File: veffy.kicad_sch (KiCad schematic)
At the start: 134 parts, among them CN1 XH-2AW_C2908611, J1 SWD, J2 Conn_Coaxial, J3 USB_C_Receptacle_USB2.0_14P, Q1 2N7002, Q2 BFR93A, Q3 2N7002, Q4 BFR93AE6327HTSA1, SW1 SW_Push, SW2 SW_Push, U1 ATSAMD21G18A-A, U10 MC34063AD, U11 AP2112K-3.3, U2 ADF4112BCPZ, U3 SA612AN/01_112, U4 MC3361, U5 LM386, U6 LM358_DFN, U7 AD9834, U8 QPA9510, U9 MCP73831-2-OT, Y2 C7527392

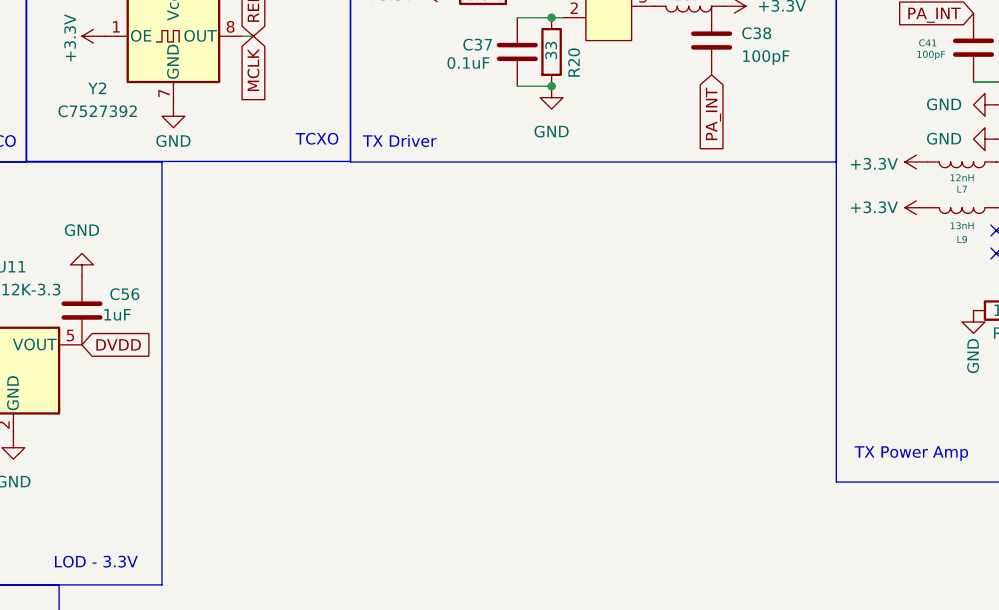
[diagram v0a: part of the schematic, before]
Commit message: TX Bandpass filter done
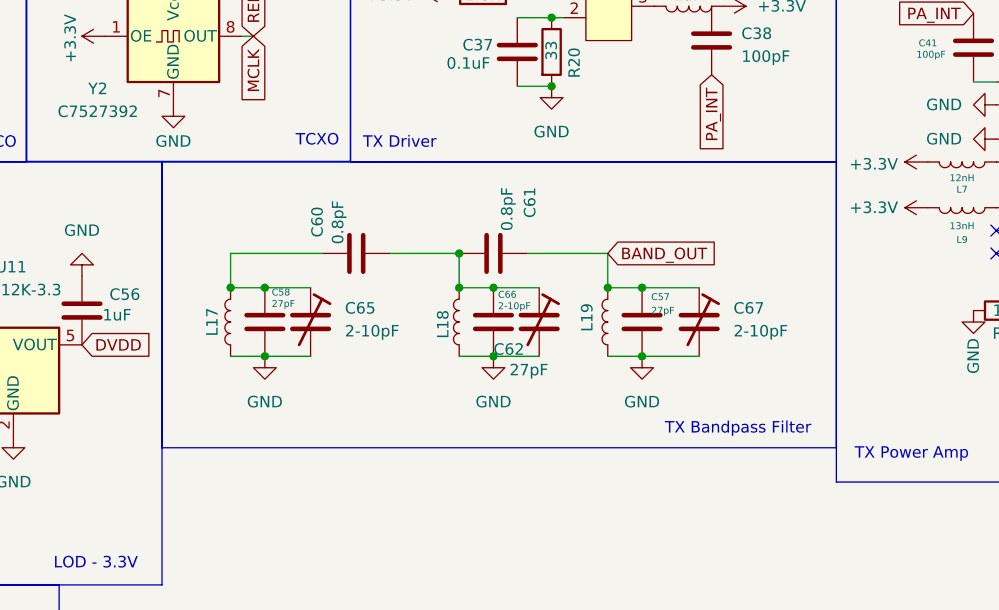
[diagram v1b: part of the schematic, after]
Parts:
- added C57, C58, C62: 27pF, symbol Device:C
- added C60, C61: 0.8pF, symbol Device:C
- added C65, C66, C67: 2-10pF, symbol Device:C_Trim
- added L17, L18, L19: 0603CS-33NXJLW, symbol Device:L
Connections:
- net BAND_OUT: now also C57.1, C61.1, C67.1, L19.2
- net GND: now also C57.2, C58.2, C62.2, C65.2, C66.2, C67.2, L17.1, L18.1, L19.1
- new net: C60.1, C61.2, C62.1, C66.1, L18.2
- new net: C58.1, C60.2, C65.1, L17.2
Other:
- note added: "TX Bandpass Filter"

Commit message: schematic fixes
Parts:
- added unit 1 of U6
- added unit 3 of U6
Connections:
- net +3.3V: now also C38.1, U6.8 (V+)
- net GND: now also C42.2, U6.3 (+), U6.4 (V-)
- net PRE_AMP: now also U6.7; no longer U6.1
- net RX_MIX_INT: now also U3.1 (INPUTA)
- net SPEAKER: now also R4.1
- net at R6.1, R7.1: now also U6.6 (-); no longer U6.2 (-)
- net at C19.1, L2.2: now also C42.1
- net at C25.2: now also U6.5 (+); no longer U6.3 (+)
- net at C22.1: now also U5.5
- new net: U6.1, U6.2 (-)
- no-connect marks 16 -> 17
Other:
- moved on the sheet: C16, C17, C18, C19, C23, C24, C38, C50, L16, L2, R4, U4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

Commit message: fixes
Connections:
- net +3.3V: no longer C38.1
- net IF_455K: now also C58.1, C60.2, C65.1, L17.2
- net at LRFC2.2, Q4.3: now also C38.1
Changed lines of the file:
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@@
 	)
 	(junction
+		(at 205.74 161.29)
+		(diameter 0)
+		(color 0 0 0 0)
+	)
+	(junction
 		(at 232.41 97.79)
 		(diameter 0)
@@
 	)
 	(junction
-		(at 213.36 161.29)
-		(diameter 0)
-		(color 0 0 0 0)
-	)
-	(junction
 		(at 50.8 125.73)
 		(diameter 0)
@@
 		)
 	)
+	(global_label "DVDD"
+		(shape input)
+		(at 213.36 161.29 0)
+		(fields_autoplaced yes)
+		(effects
+			(font
+				(size 1.27 1.27)
+			)
+			(justify left)
+		)
+		(property "Intersheetrefs" "${INTERSHEET_REFS}"
+			(at 221.2438 161.29 0)
+			(hide yes)
+			(show_name no)
+			(do_not_autoplace no)
+			(effects
+				(font
+					(size 1.27 1.27)
+				)
+				(justify left)
+			)
+		)
+	)
 	(global_label "VCO_OUT"
 		(shape input)
@@
 		)
 	)
+	(global_label "PA_INT"
+		(shape input)
+		(at 205.74 168.91 270)
+		(fields_autoplaced yes)
+		(effects
+			(font
+				(size 1.27 1.27)
+			)
+			(justify right)
+		)
+		(property "Intersheetrefs" "${INTERSHEET_REFS}"
+			(at 205.74 178.1243 90)
+			(hide yes)
+			(show_name no)
+			(do_not_autoplace no)
+			(effects
+				(font
+					(size 1.27 1.27)
+				)
+				(justify right)
+			)
+		)
+	)
 	(global_label "TX_EN"
 		(shape input)
@@
 		)
 	)
+	(global_label "IF_455K"
+		(shape input)
+		(at 158.75 189.23 90)
+		(fields_autoplaced yes)
+		(effects
+			(font
+				(size 1.27 1.27)
+			)
+			(justify left)
+		)
+		(property "Intersheetrefs" "${INTERSHEET_REFS}"
+			(at 158.75 178.6853 90)
+			(hide yes)
+			(show_name no)
+			(do_not_autoplace no)
+			(effects
+				(font
+					(size 1.27 1.27)
+				)
+				(justify left)
+			)
+		)
+	)
 	(global_label "REFIN"
 		(shape input)
@@
 		)
 	)
-	(global_label "PA_INT"
-		(shape input)
-		(at 213.36 168.91 270)
-		(fields_autoplaced yes)
-		(effects
-			(font
-				(size 1.27 1.27)
-			)
-			(justify right)
-		)
-		(property "Intersheetrefs" "${INTERSHEET_REFS}"
-			(at 213.36 178.1243 90)
-			(hide yes)
-			(show_name no)
-			(do_not_autoplace no)
-			(effects
-				(font
-					(size 1.27 1.27)
-				)
-				(justify right)
-			)
-		)
-	)
 	(global_label "VCO_OUT"
 		(shape input)
@@
 	)
 	(symbol
-		(lib_id "Device:C")
-		(at 213.36 165.1 0)
-		(unit 1)
-		(body_style 1)
-		(exclude_from_sim no)
-		(in_bom yes)
-		(on_board yes)
-		(in_pos_files yes)
-		(dnp no)
-		(property "Reference" "C38"
-			(at 216.662 164.338 0)
-			(show_name no)
-			(do_not_autoplace no)
-			(effects
-				(font
-					(size 1.27 1.27)
-				)
-				(justify left)
-			)
-		)
-		(property "Value" "100pF"
-			(at 216.662 166.878 0)
-			(show_name no)
-			(do_not_autoplace no)
-			(effects
-				(font
-					(size 1.27 1.27)
-				)
-				(justify left)
-			)
-		)
-		(property "Footprint" "Capacitor_SMD:C_0603_1608Metric_Pad1.08x0.95mm_HandSolder"
-			(at 214.3252 168.91 0)
-			(hide yes)
-			(show_name no)
-			(do_not_autoplace no)
-			(effects
-				(font
-					(size 1.27 1.27)
-				)
-			)
-		)
-		(property "Datasheet" ""
-			(at 213.36 165.1 0)
-			(hide yes)
-			(show_name no)
-			(do_not_autoplace no)
-			(effects
-				(font
-					(size 1.27 1.27)
-				)
-			)
-		)
-		(property "Description" "Unpolarized capacitor"
-			(at 213.36 165.1 0)
-			(hide yes)
-			(show_name no)
-			(do_not_autoplace no)
-			(effects
-				(font
-					(size 1.27 1.27)
-				)
-			)
-		)
-		(pin "2"
-		)
-		(pin "1"
-		)
-		(instances
-			(project "veffy"
-				(path "/a4a921cd-bed4-4c43-940c-649e397b4b90"
-					(reference "C38")
-					(unit 1)
-				)
-			)
-		)
-	)
-	(symbol
 		(lib_id "power:GND")
 		(at 234.95 97.79 0)
@@
 	(symbol
 		(lib_id "power:+3.3V")
-		(at 213.36 161.29 270)
-		(unit 1)
-		(body_style 1)
-		(exclude_from_sim no)
-		(in_bom yes)
-		(on_board yes)
-		(in_pos_files yes)
-		(dnp no)
-		(fields_autoplaced yes)
-		(property "Reference" "#PWR078"
-			(at 209.55 161.29 0)
-			(hide yes)
-			(show_name no)
-			(do_not_autoplace no)
-			(effects
-				(font
-					(size 1.27 1.27)
-				)
-			)
-		)
-		(property "Value" "+3.3V"
-			(at 217.17 161.2899 90)
-			(show_name no)
-			(do_not_autoplace no)
-			(effects
-				(font
-					(size 1.27 1.27)
-				)
-				(justify left)
-			)
-		)
-		(property "Footprint" ""
-			(at 213.36 161.29 0)
-			(hide yes)
-			(show_name no)
-			(do_not_autoplace no)
-			(effects
-				(font
-					(size 1.27 1.27)
-				)
-			)
-		)
-		(property "Datasheet" ""
-			(at 213.36 161.29 0)
-			(hide yes)
-			(show_name no)
-			(do_not_autoplace no)
-			(effects
-				(font
-					(size 1.27 1.27)
-				)
-			)
-		)
-		(property "Description" "Power symbol creates a global label with name \"+3.3V\""
-			(at 213.36 161.29 0)
-			(hide yes)
-			(show_name no)
-			(do_not_autoplace no)
-			(effects
-				(font
-					(size 1.27 1.27)
-				)
-			)
-		)
-		(pin "1"
-		)
-		(instances
-			(project "veffy"
-				(path "/a4a921cd-bed4-4c43-940c-649e397b4b90"
-					(reference "#PWR078")
-					(unit 1)
-				)
-			)
-		)
-	)
-	(symbol
-		(lib_id "power:+3.3V")
 		(at 88.9 123.19 90)
 		(unit 1)
@@
 					(unit 1)
 				)
+			)
+		)
+	)
+	(symbol
+		(lib_id "Device:C")
+		(at 205.74 165.1 0)
+		(unit 1)
+		(body_style 1)
+		(exclude_from_sim no)
+		(in_bom yes)
+		(on_board yes)
+		(in_pos_files yes)
+		(dnp no)
+		(property "Reference" "C38"
+			(at 209.042 164.338 0)
+			(show_name no)
+			(do_not_autoplace no)
+			(effects
+				(font
+					(size 1.27 1.27)
+				)
+				(justify left)
+			)
+		)
+		(property "Value" "100pF"
+			(at 209.042 166.878 0)
+			(show_name no)
+			(do_not_autoplace no)
+			(effects
+				(font
+					(size 1.27 1.27)
+				)
+				(justify left)
+			)
+		)
+		(property "Footprint" "Capacitor_SMD:C_0603_1608Metric_Pad1.08x0.95mm_HandSolder"
+			(at 206.7052 168.91 0)
+			(hide yes)
+			(show_name no)
+			(do_not_autoplace no)
+			(effects
+				(font
+					(size 1.27 1.27)
+				)
+			)
+		)
+		(property "Datasheet" ""
+			(at 205.74 165.1 0)
+			(hide yes)
+			(show_name no)
+			(do_not_autoplace no)
+			(effects
+				(font
+					(size 1.27 1.27)
+				)
+			)
+		)
+		(property "Description" "Unpolarized capacitor"
+			(at 205.74 165.1 0)
+			(hide yes)
+			(show_name no)
+			(do_not_autoplace no)
+			(effects
+				(font
+					(size 1.27 1.27)
+				)
+			)
+		)
+		(pin "2"
+		)
+		(pin "1"
+		)
+		(instances
+			(project "veffy"
+				(path "/a4a921cd-bed4-4c43-940c-649e397b4b90"
+					(reference "C38")
+					(unit 1)
+				)

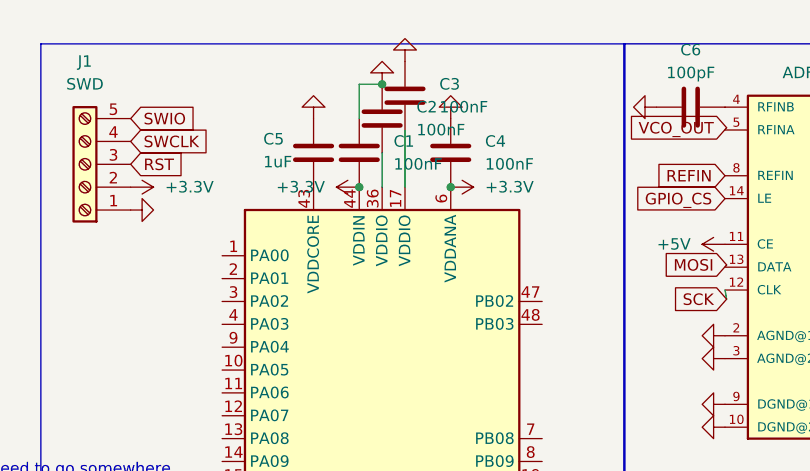
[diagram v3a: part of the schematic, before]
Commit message: Power for U1 is fixed
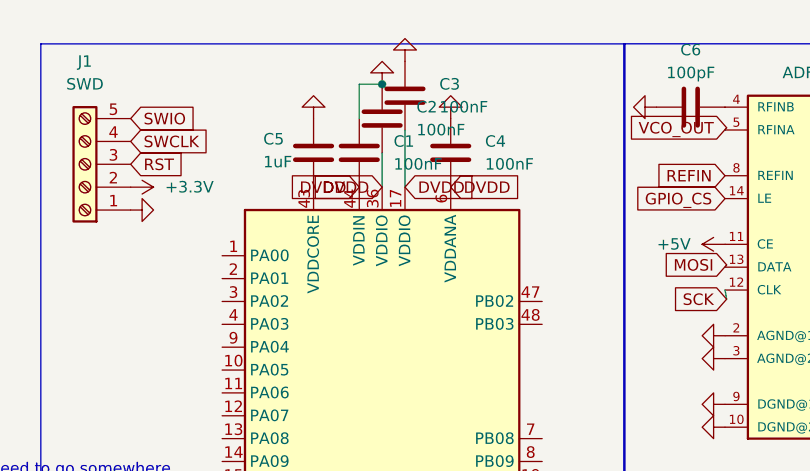
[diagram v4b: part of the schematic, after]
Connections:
- net +3.3V: now also C2.2, C3.2, U1.17 (VDDIO), U1.36 (VDDIO)
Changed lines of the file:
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@@
 	)
 	(junction
-		(at 57.15 27.94)
-		(diameter 0)
-		(color 0 0 0 0)
-	)
-	(junction
 		(at 96.52 154.94)
 		(diameter 0)
@@
 	)
 	(junction
-		(at 46.99 27.94)
-		(diameter 0)
-		(color 0 0 0 0)
-	)
-	(junction
 		(at 88.9 160.02)
 		(diameter 0)
@@
 	(global_label "DVDD"
 		(shape input)
+		(at 49.53 27.94 180)
+		(fields_autoplaced yes)
+		(effects
+			(font
+				(size 1.27 1.27)
+			)
+			(justify right)
+		)
+		(property "Intersheetrefs" "${INTERSHEET_REFS}"
+			(at 41.6462 27.94 0)
+			(hide yes)
+			(show_name no)
+			(do_not_autoplace no)
+			(effects
+				(font
+					(size 1.27 1.27)
+				)
+				(justify right)
+			)
+		)
+	)
+	(global_label "DVDD"
+		(shape input)
 		(at 232.41 60.96 180)
 		(fields_autoplaced yes)
@@
 		)
 	)
+	(global_label "DVDD"
+		(shape input)
+		(at 57.15 27.94 0)
+		(fields_autoplaced yes)
+		(effects
+			(font
+				(size 1.27 1.27)
+			)
+			(justify left)
+		)
+		(property "Intersheetrefs" "${INTERSHEET_REFS}"
+			(at 65.0338 27.94 0)
+			(hide yes)
+			(show_name no)
+			(do_not_autoplace no)
+			(effects
+				(font
+					(size 1.27 1.27)
+				)
+				(justify left)
+			)
+		)
+	)
 	(global_label "SWCLK"
 		(shape input)
@@
 		)
 	)
+	(global_label "DVDD"
+		(shape input)
+		(at 46.99 27.94 180)
+		(fields_autoplaced yes)
+		(effects
+			(font
+				(size 1.27 1.27)
+			)
+			(justify right)
+		)
+		(property "Intersheetrefs" "${INTERSHEET_REFS}"
+			(at 39.1062 27.94 0)
+			(hide yes)
+			(show_name no)
+			(do_not_autoplace no)
+			(effects
+				(font
+					(size 1.27 1.27)
+				)
+				(justify right)
+			)
+		)
+	)
 	(global_label "MCLK"
 		(shape input)
@@
 		)
 	)
+	(global_label "DVDD"
+		(shape input)
+		(at 52.07 27.94 0)
+		(fields_autoplaced yes)
+		(effects
+			(font
+				(size 1.27 1.27)
+			)
+			(justify left)
+		)
+		(property "Intersheetrefs" "${INTERSHEET_REFS}"
+			(at 59.9538 27.94 0)
+			(hide yes)
+			(show_name no)
+			(do_not_autoplace no)
+			(effects
+				(font
+					(size 1.27 1.27)
+				)
+				(justify left)
+			)
+		)
+	)
 	(global_label "SCK"
 		(shape input)
@@
 	)
 	(symbol
-		(lib_id "power:+3.3V")
-		(at 46.99 27.94 90)
-		(unit 1)
-		(body_style 1)
-		(exclude_from_sim no)
-		(in_bom yes)
-		(on_board yes)
-		(in_pos_files yes)
-		(dnp no)
-		(fields_autoplaced yes)
-		(property "Reference" "#PWR05"
-			(at 50.8 27.94 0)
-			(hide yes)
-			(show_name no)
-			(do_not_autoplace no)
-			(effects
-				(font
-					(size 1.27 1.27)
-				)
-			)
-		)
-		(property "Value" "+3.3V"
-			(at 43.18 27.9399 90)
-			(show_name no)
-			(do_not_autoplace no)
-			(effects
-				(font
-					(size 1.27 1.27)
-				)
-				(justify left)
-			)
-		)
-		(property "Footprint" ""
-			(at 46.99 27.94 0)
-			(hide yes)
-			(show_name no)
-			(do_not_autoplace no)
-			(effects
-				(font
-					(size 1.27 1.27)
-				)
-			)
-		)
-		(property "Datasheet" ""
-			(at 46.99 27.94 0)
-			(hide yes)
-			(show_name no)
-			(do_not_autoplace no)
-			(effects
-				(font
-					(size 1.27 1.27)
-				)
-			)
-		)
-		(property "Description" "Power symbol creates a global label with name \"+3.3V\""
-			(at 46.99 27.94 0)
-			(hide yes)
-			(show_name no)
-			(do_not_autoplace no)
-			(effects
-				(font
-					(size 1.27 1.27)
-				)
-			)
-		)
-		(pin "1"
-		)
-		(instances
-			(project "veffy"
-				(path "/a4a921cd-bed4-4c43-940c-649e397b4b90"
-					(reference "#PWR05")
-					(unit 1)
-				)
-			)
-		)
-	)
-	(symbol
 		(lib_id "Device:C")
 		(at 83.82 80.01 180)
@@
 					(unit 1)
 				)
-			)
-		)
-	)
-	(symbol
-		(lib_id "power:+3.3V")
-		(at 57.15 27.94 270)
-		(unit 1)
-		(body_style 1)
-		(exclude_from_sim no)
-		(in_bom yes)
-		(on_board yes)
-		(in_pos_files yes)
-		(dnp no)
-		(fields_autoplaced yes)
-		(property "Reference" "#PWR06"
-			(at 53.34 27.94 0)
-			(hide yes)
-			(show_name no)
-			(do_not_autoplace no)
-			(effects
-				(font
-					(size 1.27 1.27)
-				)
-			)
-		)
-		(property "Value" "+3.3V"
-			(at 60.96 27.9399 90)
-			(show_name no)
-			(do_not_autoplace no)
-			(effects
-				(font
-					(size 1.27 1.27)
-				)
-				(justify left)
-			)
-		)
-		(property "Footprint" ""
-			(at 57.15 27.94 0)
-			(hide yes)
-			(show_name no)
-			(do_not_autoplace no)
-			(effects
-				(font
-					(size 1.27 1.27)
-				)
-			)
-		)
-		(property "Datasheet" ""
-			(at 57.15 27.94 0)
-			(hide yes)
-			(show_name no)
-			(do_not_autoplace no)
-			(effects
-				(font
-					(size 1.27 1.27)
-				)
-			)
-		)
-		(property "Description" "Power symbol creates a global label with name \"+3.3V\""
-			(at 57.15 27.94 0)
-			(hide yes)
-			(show_name no)
-			(do_not_autoplace no)
-			(effects
-				(font
-					(size 1.27 1.27)
-				)
-			)
-		)
-		(pin "1"
-		)
-		(instances
-			(project "veffy"
-				(path "/a4a921cd-bed4-4c43-940c-649e397b4b90"
-					(reference "#PWR06")
-					(unit 1)
-				)

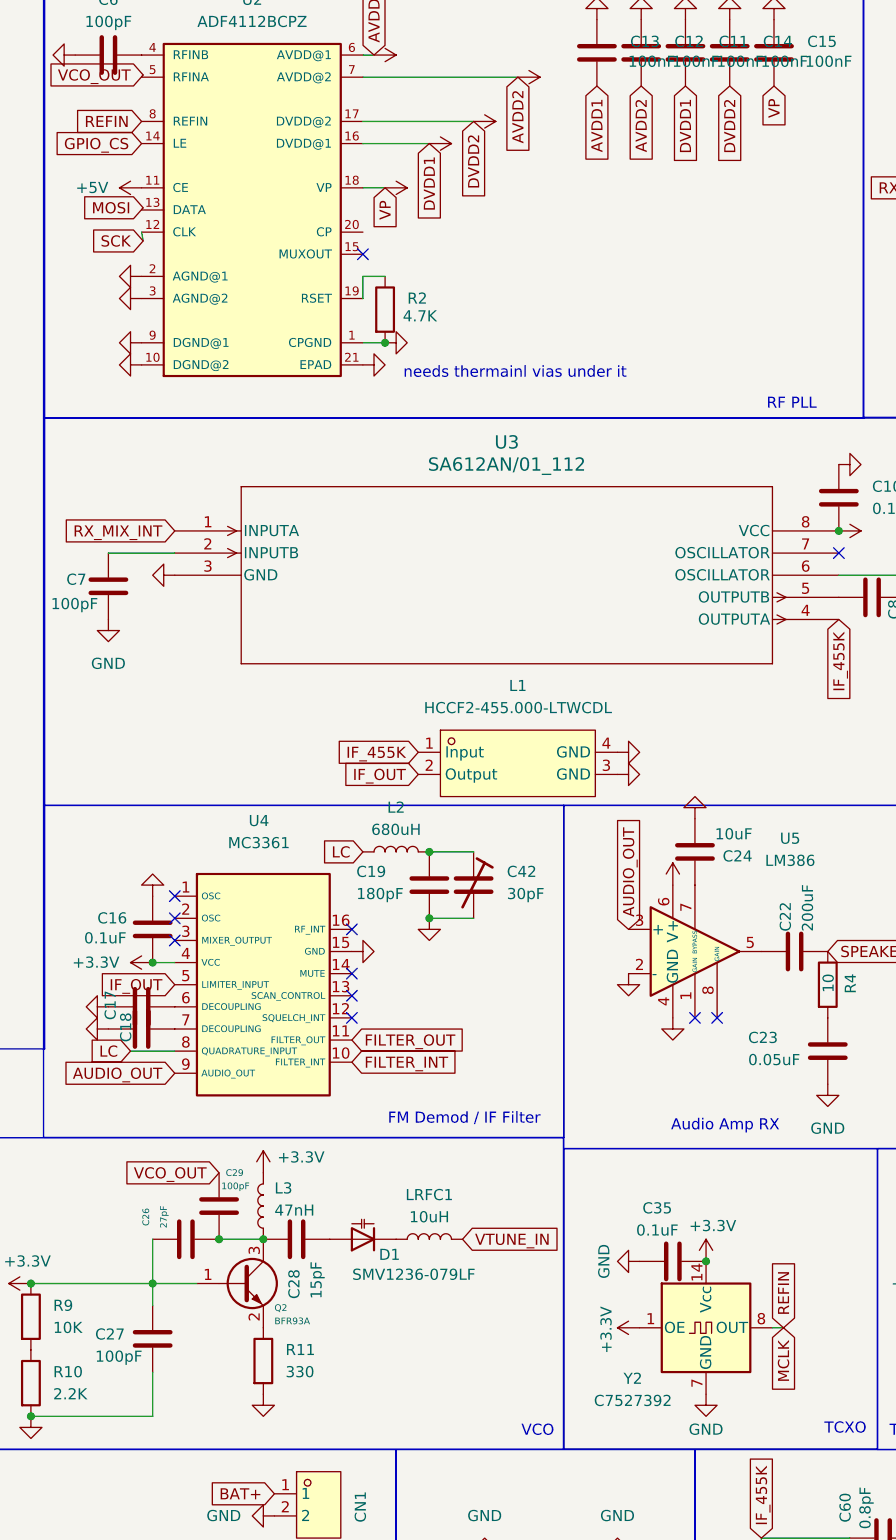
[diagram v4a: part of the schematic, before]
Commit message: VCO tank is fixed and PLL loop is finished
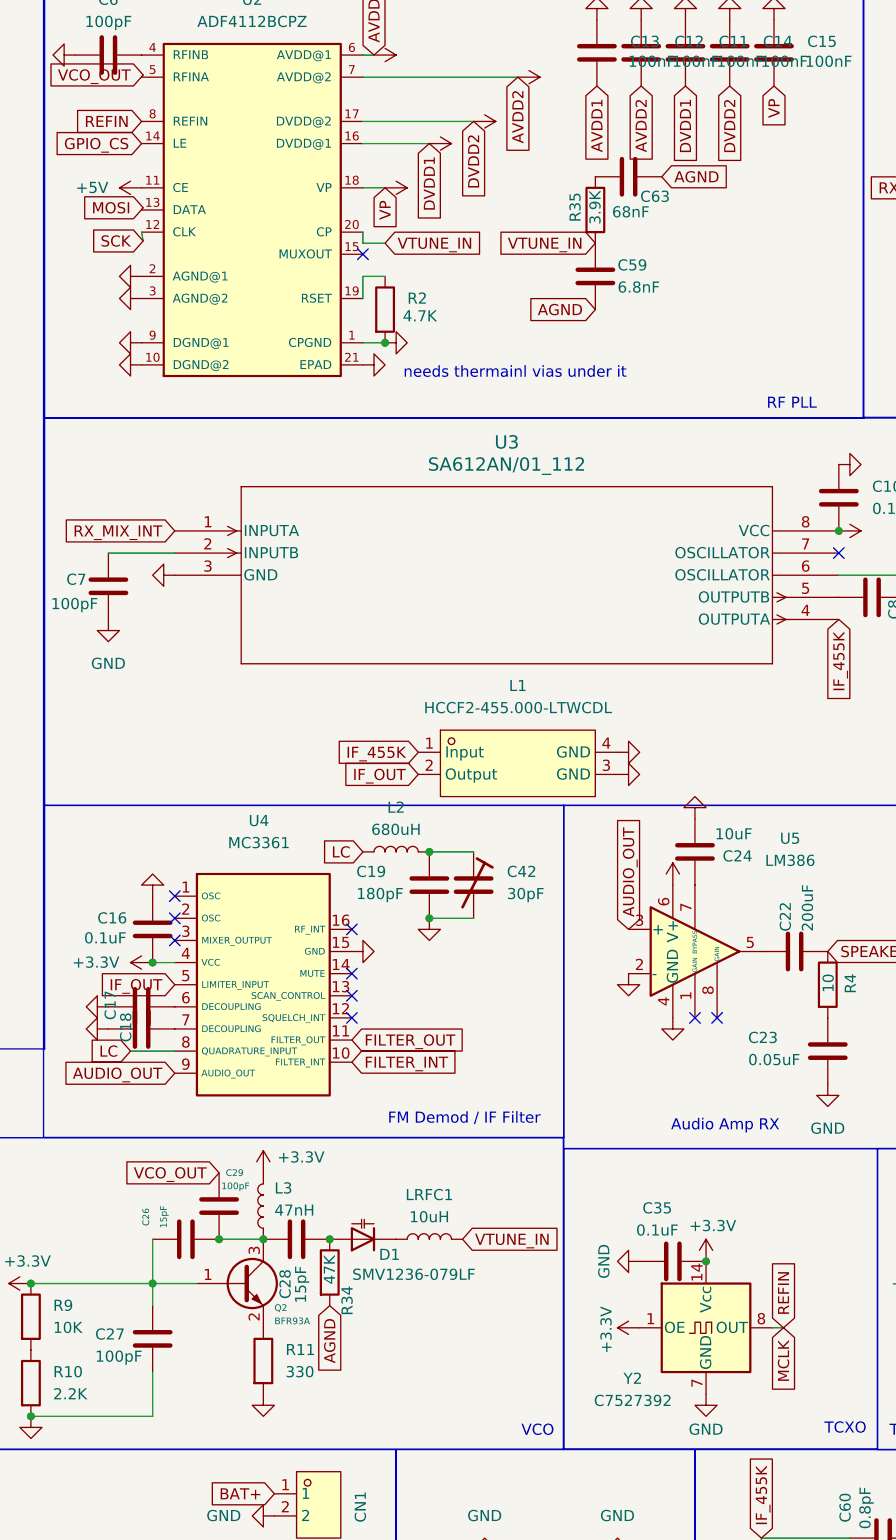
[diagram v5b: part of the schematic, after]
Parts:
- added C59: 6.8nF, symbol Device:C
- added C63: 68nF, symbol Device:C
- added R34: 47K, symbol Device:R
- added R35: 3.9K, symbol Device:R
- C26: value 27pF -> 15pF
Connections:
- net GND: now also C59.2, C63.1, R34.2
- net VTUNE_IN: now also U2.20 (CP), C59.1, R35.2
- net at C28.2, D1.2 (A): now also R34.1
- new net: C63.2, R35.1
